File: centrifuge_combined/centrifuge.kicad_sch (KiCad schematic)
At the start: 4 parts, among them J504 FPGA eXtra, J518 FPGA 6XTRA, J519 FPGA EXTR4

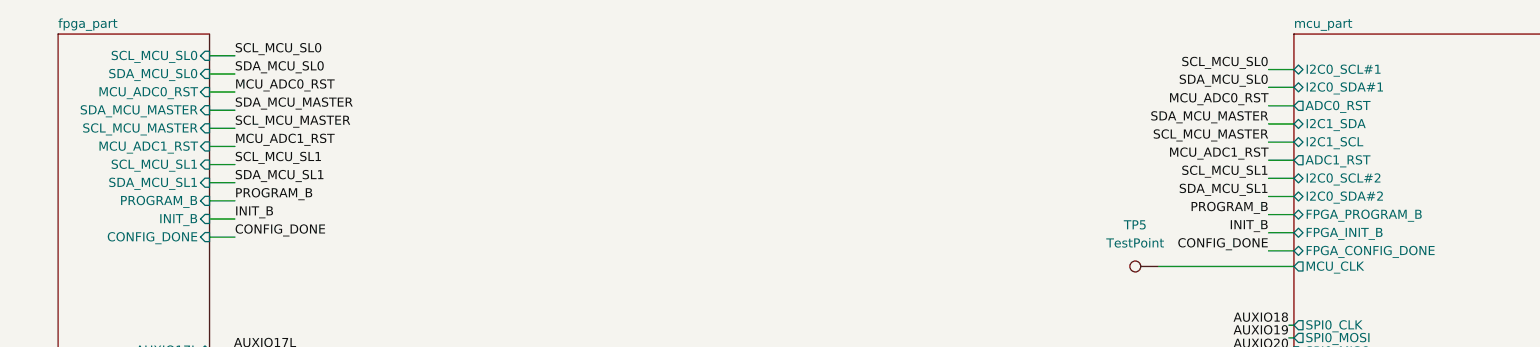
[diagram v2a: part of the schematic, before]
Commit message: change resistor values to have to 2k2, and also make I2C hopefully work
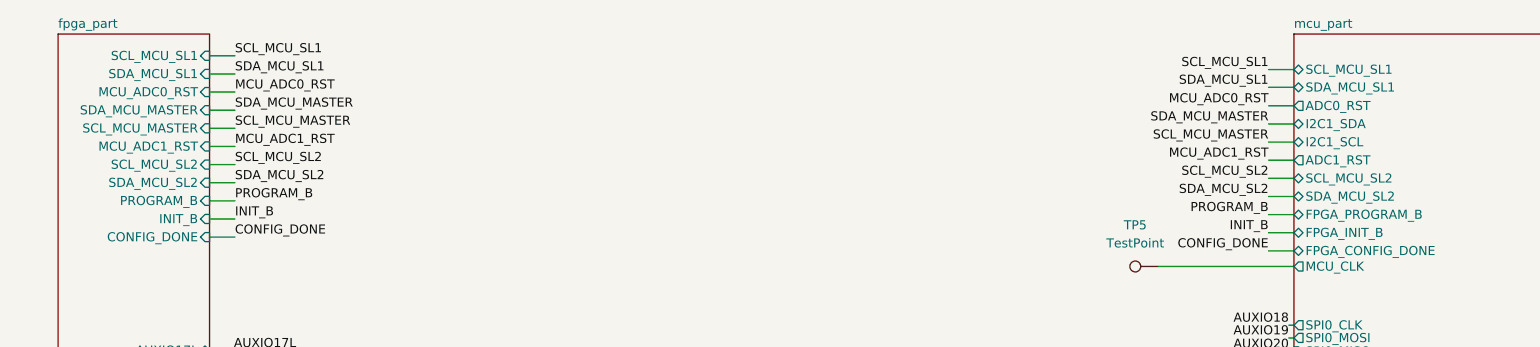
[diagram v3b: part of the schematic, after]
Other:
- sheet fpga_part ports: added SCL_MCU_SL2, SDA_MCU_SL2; removed SCL_MCU_SL0, SDA_MCU_SL0
- sheet mcu_part ports: added SCL_MCU_SL1, SCL_MCU_SL2, SDA_MCU_SL1, SDA_MCU_SL2; removed I2C0_SCL#1, I2C0_SCL#2, I2C0_SDA#1, I2C0_SDA#2

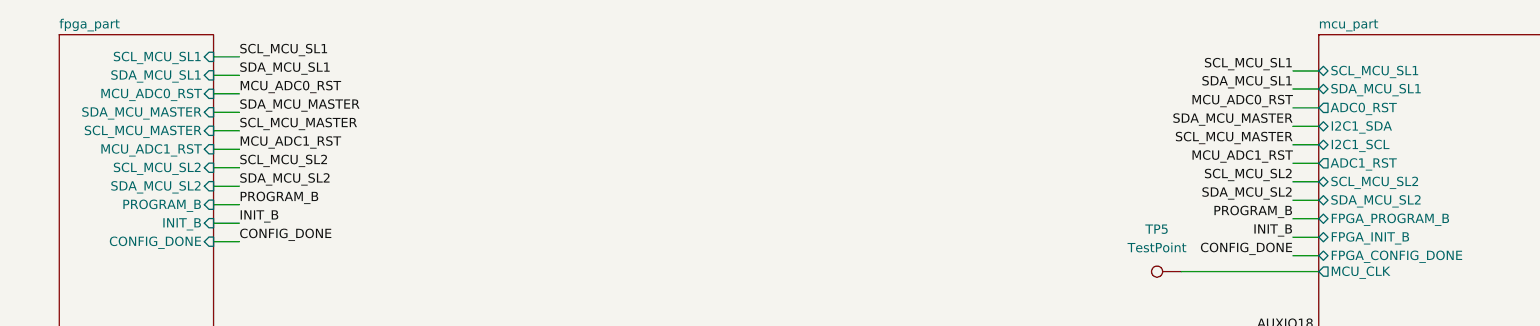
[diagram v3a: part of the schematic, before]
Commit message: change the names of some named wires in the schematic, to make numbering more consistent
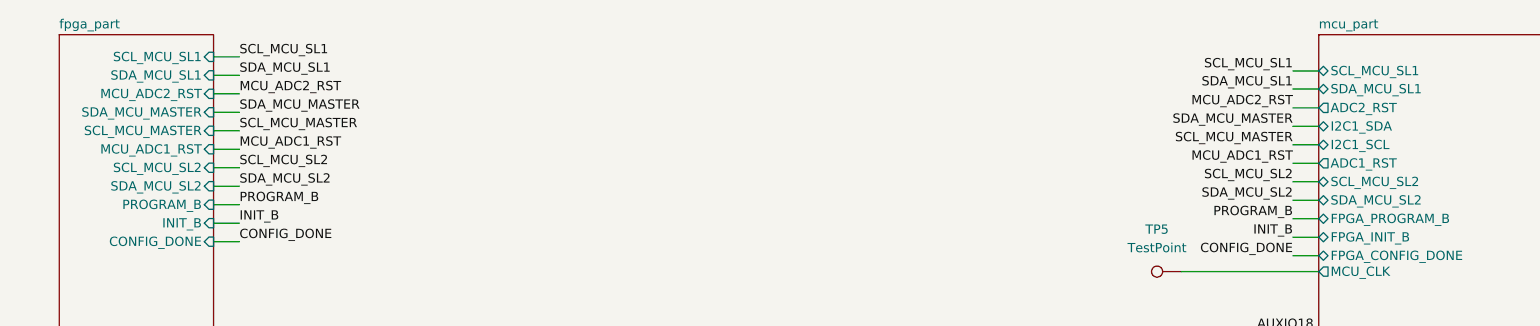
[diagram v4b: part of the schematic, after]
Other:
- sheet fpga_part ports: added MCU_ADC2_RST; removed MCU_ADC0_RST
- sheet mcu_part ports: added ADC2_RST; removed ADC0_RST
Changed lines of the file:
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@@
     (effects (font (size 1.27 1.27)) (justify right bottom))
   )
-  (label "MCU_ADC0_RST" (at 238.9124 36.7284 180)
+  (label "MCU_ADC2_RST" (at 238.9124 36.7284 180)
     (effects (font (size 1.27 1.27)) (justify right bottom))
   )
@@
     (effects (font (size 1.27 1.27)) (justify right bottom))
   )
-  (label "MCU_ADC0_RST" (at 94.107 34.798 0)
+  (label "MCU_ADC2_RST" (at 94.107 34.798 0)
     (effects (font (size 1.27 1.27)) (justify left bottom))
   )
@@
       (effects (font (size 1.27 1.27)) (justify left))
     )
-    (pin "ADC0_RST" output (at 242.4684 36.7284 180)
+    (pin "ADC2_RST" output (at 242.4684 36.7284 180)
       (effects (font (size 1.27 1.27)) (justify left))
     )
@@
       (effects (font (size 1.27 1.27)) (justify right))
     )
-    (pin "MCU_ADC0_RST" input (at 90.551 34.798 0)
-      (effects (font (size 1.27 1.27)) (justify right))
-    )
+    (pin "MCU_ADC2_RST" input (at 90.551 34.798 0)
+      (effects (font (size 1.27 1.27)) (justify right))
+    )
